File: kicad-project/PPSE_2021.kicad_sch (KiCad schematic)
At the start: 0 parts

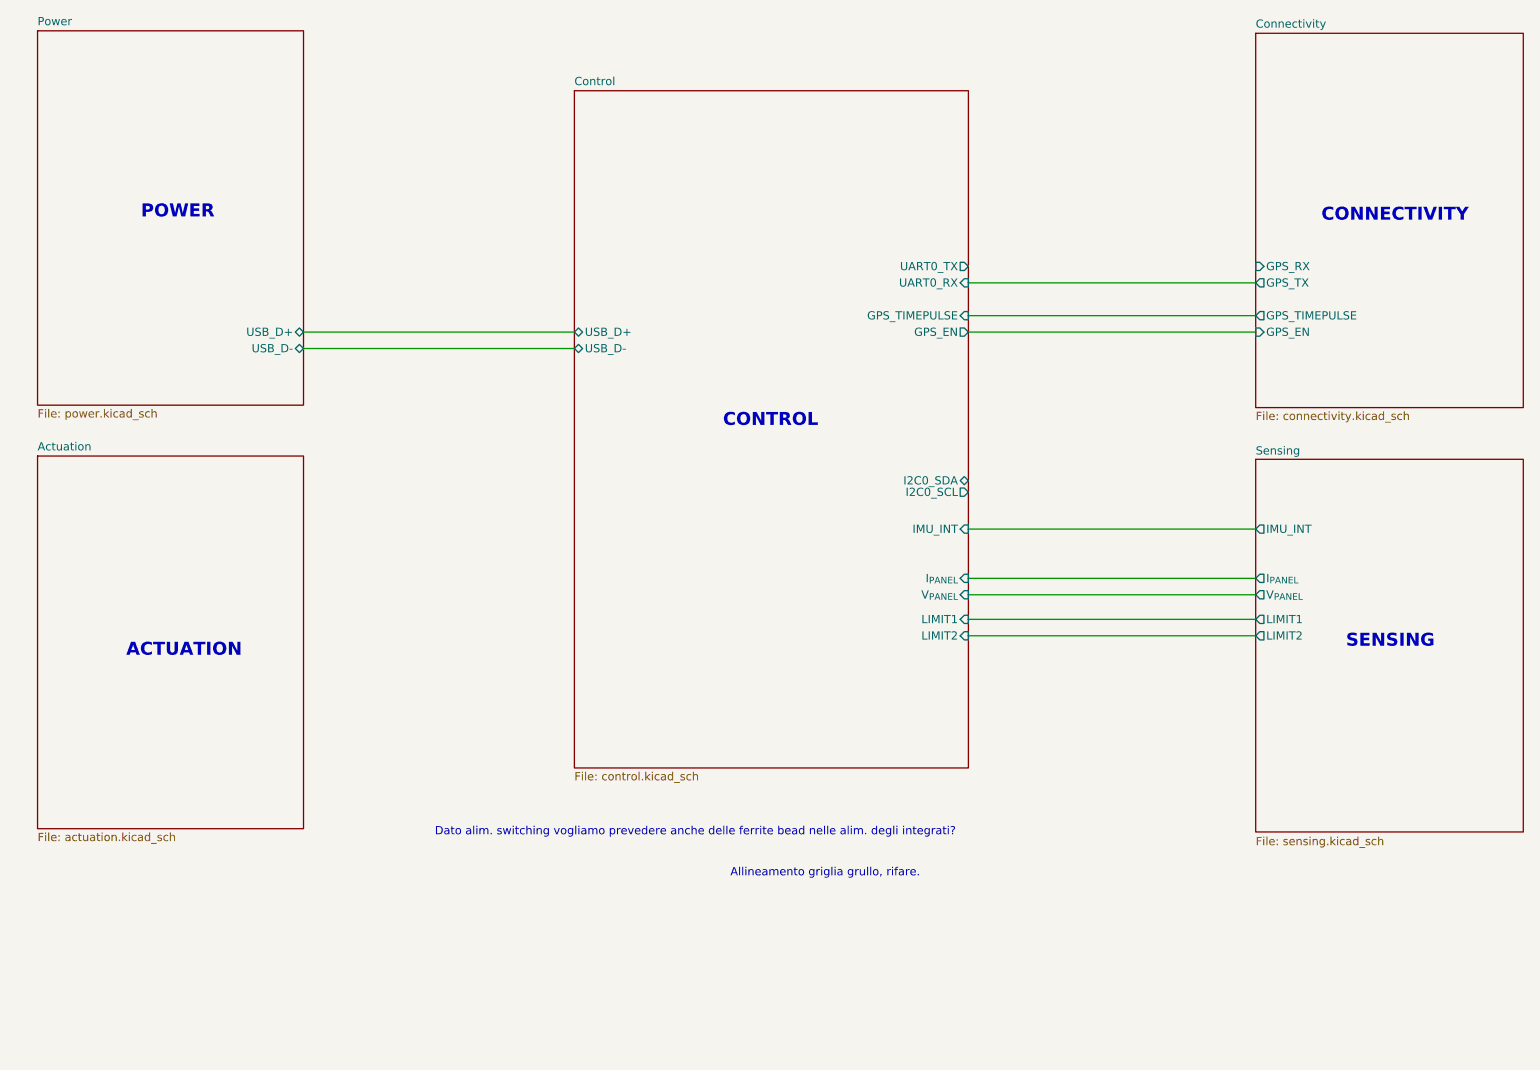
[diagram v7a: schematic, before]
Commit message: hw: add capacitor voltages, fix supply caps and other fixes
add capacitor voltages, change polarized caps to normal, move switching capacitors, remove 5V power, fix switching ballast capacitor, remove switching feedback capacitor, switch sensing and actuation sub-sheets positions in main sheet, add labels to most nodes for pcb layout, connect GPS supply caps directly, remove biased transistor and ferrite bead from GPS enable MOSFET, remove unneeded pins from stepper motors connectors
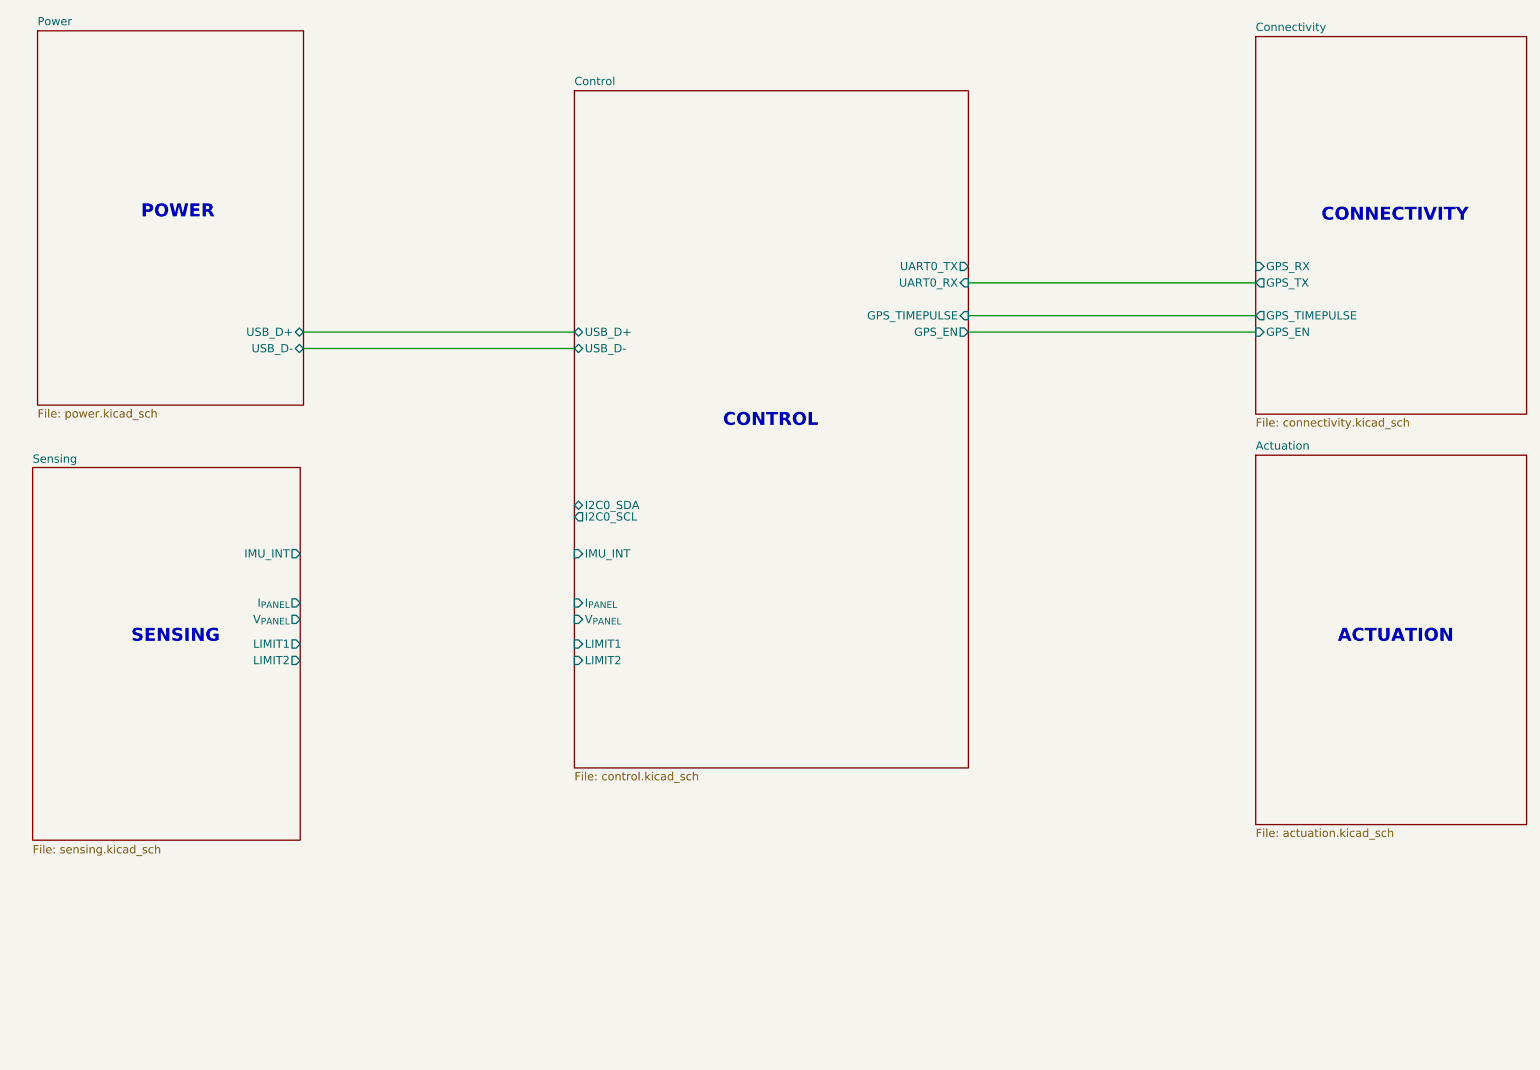
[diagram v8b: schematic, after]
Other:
- note removed: "Allineamento griglia grullo, rifare."
- note removed: "Dato alim. switching vogliamo prevedere anche delle ferrite bead nelle alim. degli integrati?"
